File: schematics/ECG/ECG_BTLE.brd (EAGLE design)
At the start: 25.4 x 25.4 mm, 6 parts, among them IC1 ADS1293, IC3 LP2985

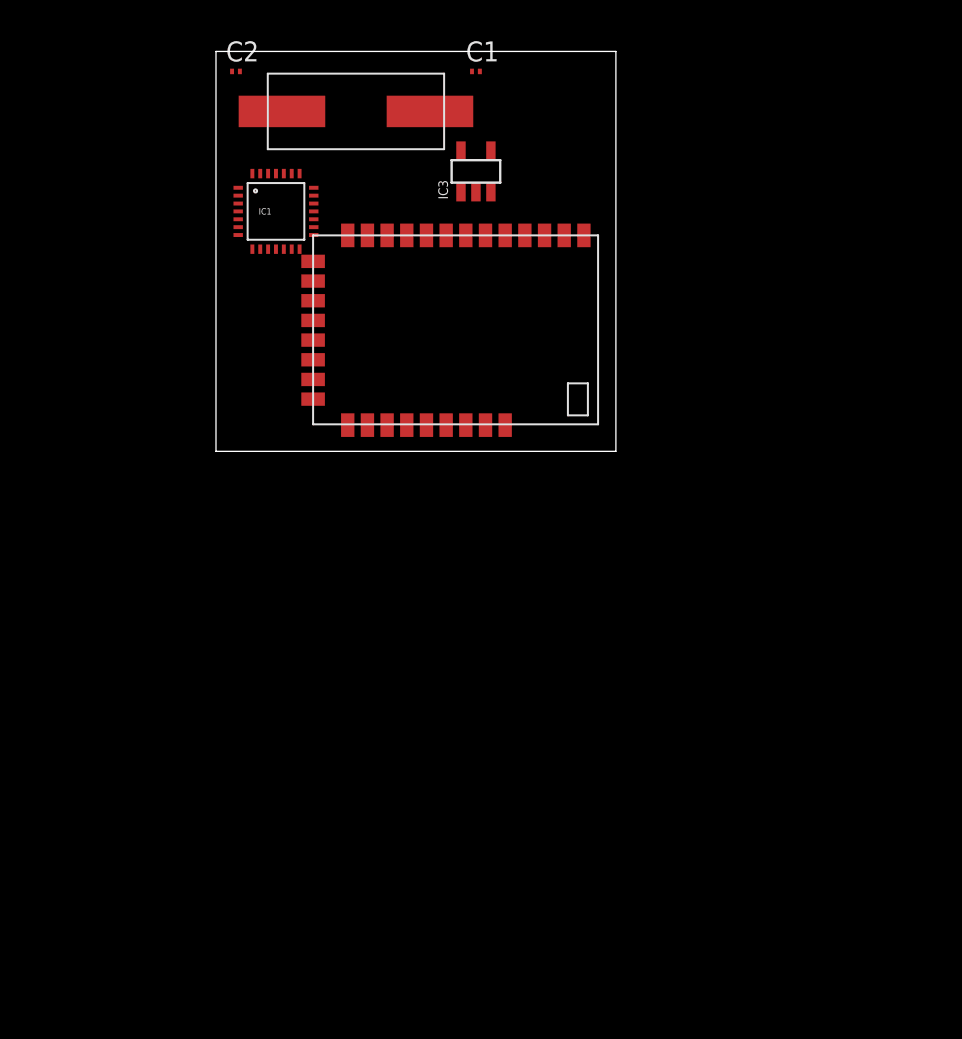
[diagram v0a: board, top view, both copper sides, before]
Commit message: schematic update
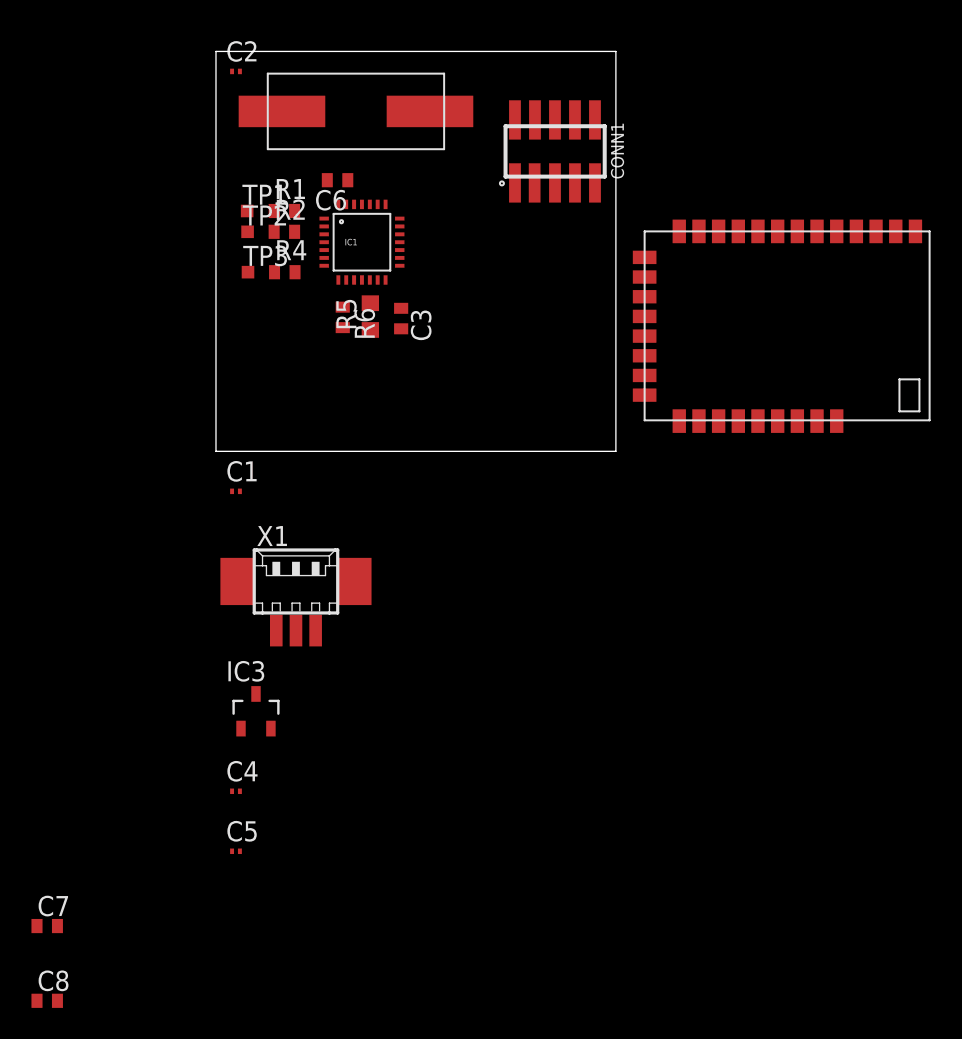
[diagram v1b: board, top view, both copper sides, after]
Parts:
- added C3: 1nF (01016D102KAT2A), rcl:C0402
- added C4, C5: 1uF, rcl:C0201
- added C6: 1uF (C1005X7S0J105K), rcl:C0402
- added C7, C8: 0.1uF, rcl:C0402
- added CONN1: 10POS_1.27MM_SMD, harwin:1.27MM_SMD
- added R1, R2, R4: 0, resistor:R0402
- added R5: 10M (RK73H1HTTC1005F), resistor:R0603
- added R6: 10K (RK73B1FTTBL103J), resistor:R0402
- added TP1, TP2, TP3: TPSTP08SQ, testpad:TP08SQ
- added X1: 53261-03, con-molex:53261-03
- IC3: value LP2985 -> MCP1703; device ti:SOT23-5 -> microchip_regulators:SOT23
- moved IC3 37.0 mm to (2.54, -16.5)
- moved C1 30.7 mm to (1.27, -2.54)
- moved IC2 21.1 mm to (36.3, 7.87)
- moved IC1 5.80 mm to (9.27, 13.3)
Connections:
- new net BATT+: C4.1, IC3.3, X1.3
- new net CMOUT: IC1.8, R6.1
- new net CVREF: C6.1, IC1.26
- new net GND: C4.2, C5.2, C6.2, C7.2, C8.2, IC1.14, IC1.27, IC3.1, X1.2
- new net IN1: IC1.1, R1.2
- new net IN2: IC1.2, R2.2
- new net IN4: IC1.4, R4.2
- new net LA: R2.1, TP2.TP
- new net N$1: CONN1.4
- new net N$2: CONN1.3
- new net N$3: CONN1.7
- new net N$4: CONN1.1
- new net N$7: C5.1, IC3.2
- new net RA: R1.1, TP1.TP
- new net RL: R4.1, TP3.TP
- new net RLDINV: C3.2, IC1.10, R5.1, R6.2
- new net RLDOUT: C3.1, IC1.9, R5.2
- new net VDD: C7.1, C8.1, IC1.22, IC1.28
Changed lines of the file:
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@@
 <?xml version="1.0" encoding="utf-8"?>
 <!DOCTYPE eagle SYSTEM "eagle.dtd">
-<eagle version="6.2">
+<eagle version="6.4">
 <drawing>
 <settings>
@@
 <setting verticaltext="up"/>
 </settings>
-<grid distance="0.05" unitdist="inch" unit="inch" style="lines" multiple="1" display="no" altdistance="0.025" altunitdist="inch" altunit="inch"/>
+<grid distance="1" unitdist="mil" unit="mil" style="lines" multiple="1" display="no" altdistance="0.025" altunitdist="inch" altunit="inch"/>
 <layers>
 <layer number="1" name="Top" color="4" fill="1" visible="yes" active="yes"/>
@@
 <layer number="215" name="215bmp" color="7" fill="1" visible="yes" active="yes"/>
 <layer number="216" name="216bmp" color="7" fill="1" visible="yes" active="yes"/>
+<layer number="217" name="217bmp" color="18" fill="1" visible="no" active="no"/>
+<layer number="218" name="218bmp" color="19" fill="1" visible="no" active="no"/>
+<layer number="219" name="219bmp" color="20" fill="1" visible="no" active="no"/>
+<layer number="220" name="220bmp" color="21" fill="1" visible="no" active="no"/>
+<layer number="221" name="221bmp" color="22" fill="1" visible="no" active="no"/>
+<layer number="222" name="222bmp" color="23" fill="1" visible="no" active="no"/>
+<layer number="223" name="223bmp" color="24" fill="1" visible="no" active="no"/>
+<layer number="224" name="224bmp" color="25" fill="1" visible="no" active="no"/>
 <layer number="231" name="Eagle3D_PG1" color="14" fill="1" visible="yes" active="yes"/>
 <layer number="232" name="Eagle3D_PG2" color="14" fill="2" visible="yes" active="yes"/>
@@
 </class>
 </classes>
-<designrules>
+<designrules name="default">
 <description language="de">&lt;b&gt;EAGLE Design Rules&lt;/b&gt;
 &lt;p&gt;
@@
 </autorouter>
 <elements>
-<element name="IC1" library="texas_instruments" package="WQFN28" value="ADS1293" x="3.81" y="15.24"/>
-<element name="IC2" library="bluegiga" package="BLE112" value="" x="15.24" y="7.62" rot="R270"/>
-<element name="IC3" library="ti" package="SOT23-5" value="LP2985" x="16.51" y="17.78"/>
-<element name="C1" library="rcl" package="C0201" value="" x="16.51" y="24.13"/>
+<element name="IC1" library="texas_instruments" package="WQFN28" value="ADS1293" x="9.271" y="13.2842"/>
+<element name="IC2" library="bluegiga" package="BLE112" value="" x="36.2966" y="7.874" rot="R270"/>
 <element name="C2" library="rcl" package="C0201" value="" x="1.27" y="24.13"/>
 <element name="U$1" library="ecs" package="CSM-7" value="XTAL-CSM7" x="8.89" y="21.59"/>
+<element name="CONN1" library="harwin" package="1.27MM_SMD" value="10POS_1.27MM_SMD" x="21.59" y="19.05"/>
+<element name="C1" library="rcl" package="C0201" value="" x="1.27" y="-2.54"/>
+<element name="X1" library="con-molex" package="53261-03" value="53261-03" x="5.08" y="-8.89">
+<attribute name="OC_NEWARK" value="57H5006" x="5.08" y="-8.89" size="1.778" layer="27" display="off"/>
+<attribute name="MPN" value="53261-0390" x="5.08" y="-8.89" size="1.778" layer="27" display="off"/>
+<attribute name="MF" value="MOLEX" x="5.08" y="-8.89" size="1.778" layer="27" display="off"/>
+<attribute name="OC_FARNELL" value="1125359" x="5.08" y="-8.89" size="1.778" layer="27" display="off"/>
+</element>
+<element name="IC3" library="microchip_regulators" package="SOT23" value="MCP1703" x="2.54" y="-16.51"/>
+<element name="C4" library="rcl" package="C0201" value="1uF" x="1.27" y="-21.59"/>
+<element name="C5" library="rcl" package="C0201" value="1uF" x="1.27" y="-25.4"/>
+<element name="TP1" library="testpad" package="TP08SQ" value="TPSTP08SQ" x="1.9812" y="15.2654">
+<attribute name="TP_SIGNAL_NAME" value="" x="1.9812" y="15.2654" size="1.778" layer="27" display="off"/>
+</element>
+<element name="TP2" library="testpad" package="TP08SQ" value="TPSTP08SQ" x="2.0066" y="13.9446">
+<attribute name="TP_SIGNAL_NAME" value="" x="2.0066" y="13.9446" size="1.778" layer="27" display="off"/>
+</element>
+<element name="TP3" library="testpad" package="TP08SQ" value="TPSTP08SQ" x="2.032" y="11.3792">
+<attribute name="TP_SIGNAL_NAME" value="" x="2.032" y="11.3792" size="1.778" layer="27" display="off"/>
+</element>
+<element name="R1" library="resistor" package="R0402" value="0" x="4.3434" y="15.2654"/>
+<element name="R2" library="resistor" package="R0402" value="0" x="4.3434" y="13.9446"/>
+<element name="R4" library="resistor" package="R0402" value="0" x="4.3688" y="11.3792"/>
+<element name="C3" library="rcl" package="C0402" value="1nF (01016D102KAT2A)" x="11.7602" y="8.4328" rot="R270"/>
+<element name="R5" library="resistor" package="R0603" value="10M (RK73H1HTTC1005F)" x="9.8044" y="8.5598" rot="R90"/>
+<element name="R6" library="resistor" package="R0402" value="10K (RK73B1FTTBL103J)" x="8.0518" y="8.509" rot="R270"/>
+<element name="C6" library="rcl" package="C0402" value="1uF (C1005X7S0J105K)" x="7.7216" y="17.2212" rot="R180"/>
+<element name="C7" library="rcl" package="C0402" value="0.1uF" x="-10.7188" y="-30.1498"/>
+<element name="C8" library="rcl" package="C0402" value="0.1uF" x="-10.7188" y="-34.8996"/>
 </elements>
 <signals>
+<signal name="N$1">
+<contactref element="CONN1" pad="4"/>
+</signal>
+<signal name="N$2">
+<contactref element="CONN1" pad="3"/>
+</signal>
+<signal name="N$3">
+<contactref element="CONN1" pad="7"/>
+</signal>
+<signal name="N$4">
+<contactref element="CONN1" pad="1"/>
+</signal>
+<signal name="GND">
+<contactref element="X1" pad="2"/>
+<contactref element="IC3" pad="1"/>
+<contactref element="C4" pad="2"/>
+<contactref element="C5" pad="2"/>
+<contactref element="C6" pad="2"/>
+<contactref element="C8" pad="2"/>
+<contactref element="C7" pad="2"/>
+<contactref element="IC1" pad="27"/>
+<contactref element="IC1" pad="14"/>
+<wire x1="-10.0688" y1="-30.1498" x2="-10.0688" y2="-34.8996" width="0" layer="19" extent="1-1"/>
+<wire x1="1.52" y1="-25.4" x2="-10.0688" y2="-30.1498" width="0" layer="19" extent="1-1"/>
+<wire x1="1.52" y1="-21.59" x2="1.52" y2="-25.4" width="0" layer="19" extent="1-1"/>
+<wire x1="1.59" y1="-17.61" x2="1.52" y2="-21.59" width="0" layer="19" extent="1-1"/>
+<wire x1="5.08" y1="-11.39" x2="1.59" y2="-17.61" width="0" layer="19" extent="1-1"/>
+<wire x1="10.771" y1="10.8842" x2="5.08" y2="-11.39" width="0" layer="19" extent="1-1"/>
+<wire x1="8.271" y1="15.6842" x2="10.771" y2="10.8842" width="0" layer="19" extent="1-1"/>
+<wire x1="7.0716" y1="17.2212" x2="8.271" y2="15.6842" width="0" layer="19" extent="1-1"/>
+</signal>
+<signal name="BATT+">
+<contactref element="X1" pad="3"/>
+<contactref element="IC3" pad="3"/>
+<contactref element="C4" pad="1"/>
+<wire x1="2.54" y1="-15.41" x2="1.02" y2="-21.59" width="0" layer="19" extent="1-1"/>
+<wire x1="3.83" y1="-11.39" x2="2.54" y2="-15.41" width="0" layer="19" extent="1-1"/>
+</signal>
+<signal name="N$7">
+<contactref element="IC3" pad="2"/>
+<contactref element="C5" pad="1"/>
+<wire x1="3.49" y1="-17.61" x2="1.02" y2="-25.4" width="0" layer="19" extent="1-1"/>
+</signal>
+<signal name="IN1">
+<contactref element="IC1" pad="1"/>
+<contactref element="R1" pad="2"/>
+<wire x1="4.9934" y1="15.2654" x2="6.871" y2="14.7842" width="0" layer="19" extent="1-1"/>
+</signal>
+<signal name="IN2">
+<contactref element="IC1" pad="2"/>
+<contactref element="R2" pad="2"/>
+<wire x1="4.9934" y1="13.9446" x2="6.871" y2="14.2842" width="0" layer="19" extent="1-1"/>
+</signal>
+<signal name="IN4">
+<contactref element="IC1" pad="4"/>
+<contactref element="R4" pad="2"/>
+<wire x1="5.0188" y1="11.3792" x2="6.871" y2="13.2842" width="0" layer="19" extent="1-1"/>
+</signal>
+<signal name="RA">
+<contactref element="TP1" pad="TP"/>
+<contactref element="R1" pad="1"/>
+<wire x1="1.9812" y1="15.2654" x2="3.6934" y2="15.2654" width="0" layer="19" extent="1-1"/>
+</signal>
+<signal name="LA">
+<contactref element="TP2" pad="TP"/>
+<contactref element="R2" pad="1"/>
+<wire x1="2.0066" y1="13.9446" x2="3.6934" y2="13.9446" width="0" layer="19" extent="1-1"/>
+</signal>
+<signal name="RL">
+<contactref element="TP3" pad="TP"/>
+<contactref element="R4" pad="1"/>
+<wire x1="2.032" y1="11.3792" x2="3.7188" y2="11.3792" width="0" layer="19" extent="1-1"/>
+</signal>
+<signal name="RLDOUT">
+<contactref element="IC1" pad="9"/>
+<contactref element="C3" pad="1"/>
+<contactref element="R5" pad="2"/>
+<wire x1="9.8044" y1="9.4098" x2="8.271" y2="10.8842" width="0" layer="19" extent="1-1"/>
+<wire x1="11.7602" y1="9.0828" x2="9.8044" y2="9.4098" width="0" layer="19" extent="1-1"/>
+</signal>
+<signal name="RLDINV">
+<contactref element="IC1" pad="10"/>
+<contactref element="C3" pad="2"/>
+<contactref element="R5" pad="1"/>
+<contactref element="R6" pad="2"/>
+<wire x1="8.0518" y1="7.859" x2="8.771" y2="10.8842" width="0" layer="19" extent="1-1"/>
+<wire x1="9.8044" y1="7.7098" x2="8.0518" y2="7.859" width="0" layer="19" extent="1-1"/>
+<wire x1="11.7602" y1="7.7828" x2="9.8044" y2="7.7098" width="0" layer="19" extent="1-1"/>
+</signal>
+<signal name="CMOUT">
+<contactref element="IC1" pad="8"/>
+<contactref element="R6" pad="1"/>
+<wire x1="8.0518" y1="9.159" x2="7.771" y2="10.8842" width="0" layer="19" extent="1-1"/>
+</signal>
+<signal name="CVREF">
+<contactref element="IC1" pad="26"/>
+<contactref element="C6" pad="1"/>
+<wire x1="8.3716" y1="17.2212" x2="8.771" y2="15.6842" width="0" layer="19" extent="1-1"/>
+</signal>
+<signal name="VDD">
+<contactref element="IC1" pad="28"/>
+<contactref element="IC1" pad="22"/>
+<contactref element="C7" pad="1"/>
+<contactref element="C8" pad="1"/>
+<wire x1="-11.3688" y1="-30.1498" x2="-11.3688" y2="-34.8996" width="0" layer="19" extent="1-1"/>
+<wire x1="7.771" y1="15.6842" x2="-11.3688" y2="-30.1498" width="0" layer="19" extent="1-1"/>
+<wire x1="10.771" y1="15.6842" x2="7.771" y2="15.6842" width="0" layer="19" extent="1-1"/>
+</signal>
 </signals>
 </board>
